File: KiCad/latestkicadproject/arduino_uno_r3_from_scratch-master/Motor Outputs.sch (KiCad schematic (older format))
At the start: 8 parts

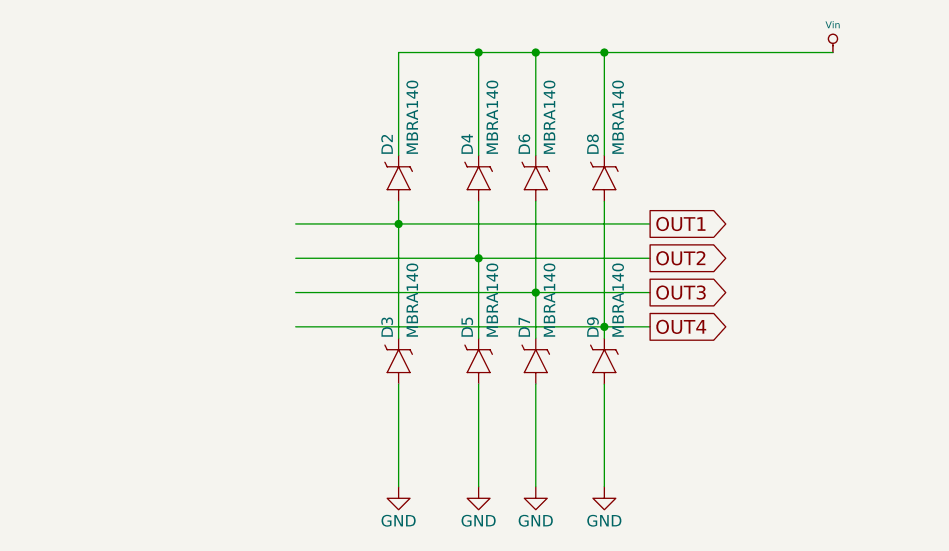
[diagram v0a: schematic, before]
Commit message: 28feb
Aanpassing KiCad+deel footprints
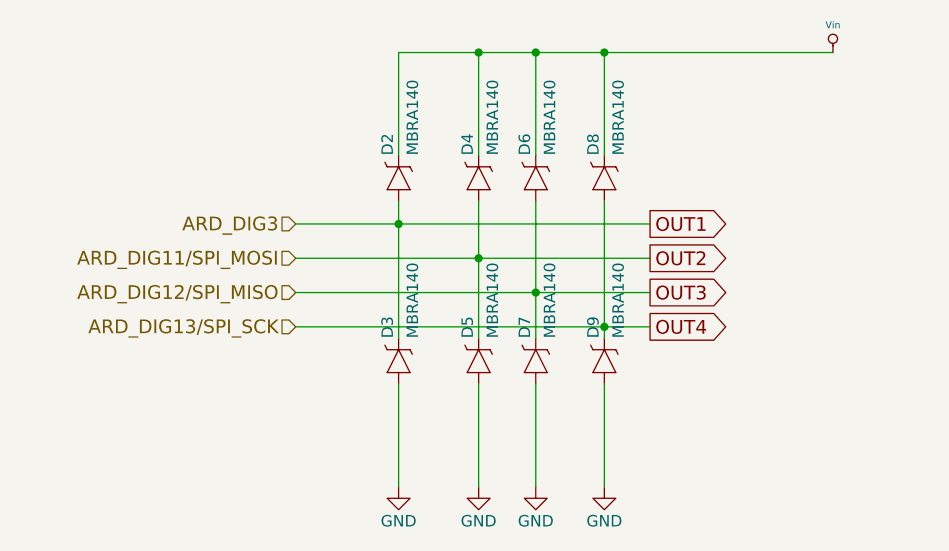
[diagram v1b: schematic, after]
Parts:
- D2, D3, D4, D5, D6, D7, D8, D9: footprint SMA-DIODE -> (none)
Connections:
- net labels added: ARD_DIG11/SPI_MOSI, ARD_DIG12/SPI_MISO, ARD_DIG13/SPI_SCK, ARD_DIG3
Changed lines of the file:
@@
 F 0 "D9" H 6100 4169 50  0000 L BNN
 F 1 "MBRA140" H 6100 4059 50  0000 L BNN
-F 2 "SMA-DIODE" H 6030 4300 20  0001 C CNN
+F 2 "" H 6030 4300 20  0001 C CNN
 F 3 "" H 6000 4150 60  0001 C CNN
 	1    6000 4150
@@
 F 0 "D7" H 5800 4169 50  0000 L BNN
 F 1 "MBRA140" H 5800 4059 50  0000 L BNN
-F 2 "SMA-DIODE" H 5730 4300 20  0001 C CNN
+F 2 "" H 5730 4300 20  0001 C CNN
 F 3 "" H 5700 4150 60  0001 C CNN
 	1    5700 4150
@@
 F 0 "D5" H 5550 4169 50  0000 L BNN
 F 1 "MBRA140" H 5550 4059 50  0000 L BNN
-F 2 "SMA-DIODE" H 5480 4300 20  0001 C CNN
+F 2 "" H 5480 4300 20  0001 C CNN
 F 3 "" H 5450 4150 60  0001 C CNN
 	1    5450 4150
@@
 F 0 "D3" H 5200 4169 50  0000 L BNN
 F 1 "MBRA140" H 5200 4059 50  0000 L BNN
-F 2 "SMA-DIODE" H 5130 4300 20  0001 C CNN
+F 2 "" H 5130 4300 20  0001 C CNN
 F 3 "" H 5100 4150 60  0001 C CNN
 	1    5100 4150
@@
 F 0 "D8" H 6100 3369 50  0000 L BNN
 F 1 "MBRA140" H 6100 3259 50  0000 L BNN
-F 2 "SMA-DIODE" H 6030 3500 20  0001 C CNN
+F 2 "" H 6030 3500 20  0001 C CNN
 F 3 "" H 6000 3350 60  0001 C CNN
 	1    6000 3350
@@
 F 0 "D6" H 5800 3369 50  0000 L BNN
 F 1 "MBRA140" H 5800 3259 50  0000 L BNN
-F 2 "SMA-DIODE" H 5730 3500 20  0001 C CNN
+F 2 "" H 5730 3500 20  0001 C CNN
 F 3 "" H 5700 3350 60  0001 C CNN
 	1    5700 3350
@@
 F 0 "D4" H 5550 3369 50  0000 L BNN
 F 1 "MBRA140" H 5550 3259 50  0000 L BNN
-F 2 "SMA-DIODE" H 5480 3500 20  0001 C CNN
+F 2 "" H 5480 3500 20  0001 C CNN
 F 3 "" H 5450 3350 60  0001 C CNN
 	1    5450 3350
@@
 F 0 "D2" H 5200 3369 50  0000 L BNN
 F 1 "MBRA140" H 5200 3259 50  0000 L BNN
-F 2 "SMA-DIODE" H 5130 3500 20  0001 C CNN
+F 2 "" H 5130 3500 20  0001 C CNN
 F 3 "" H 5100 3350 60  0001 C CNN
 	1    5100 3350
@@
 $EndComp
 $Comp
-L GND #PWR028
+L GND #PWR020
 U 1 1 5A0B3F5C
 P 5100 4700
-F 0 "#PWR028" H 5100 4450 50  0001 C CNN
+F 0 "#PWR020" H 5100 4450 50  0001 C CNN
 F 1 "GND" H 5100 4550 50  0000 C CNN
 F 2 "" H 5100 4700 50  0001 C CNN
@@
 $EndComp
 $Comp
-L GND #PWR029
+L GND #PWR021
 U 1 1 5A0B3F8E
 P 5450 4700
-F 0 "#PWR029" H 5450 4450 50  0001 C CNN
+F 0 "#PWR021" H 5450 4450 50  0001 C CNN
 F 1 "GND" H 5450 4550 50  0000 C CNN
 F 2 "" H 5450 4700 50  0001 C CNN
@@
 $EndComp
 $Comp
-L GND #PWR030
+L GND #PWR022
 U 1 1 5A0B3FB1
 P 5700 4700
-F 0 "#PWR030" H 5700 4450 50  0001 C CNN
+F 0 "#PWR022" H 5700 4450 50  0001 C CNN
 F 1 "GND" H 5700 4550 50  0000 C CNN
 F 2 "" H 5700 4700 50  0001 C CNN
@@
 $EndComp
 $Comp
-L GND #PWR031
+L GND #PWR023
 U 1 1 5A0B43FA
 P 6000 4700
-F 0 "#PWR031" H 6000 4450 50  0001 C CNN
+F 0 "#PWR023" H 6000 4450 50  0001 C CNN
 F 1 "GND" H 6000 4550 50  0000 C CNN
 F 2 "" H 6000 4700 50  0001 C CNN
@@
 Wire Wire Line
 	6000 4250 6000 4700
-Wire Wire Line
-	5450 4700 5450 4250
 Wire Wire Line
 	5700 4250 5700 4700
@@
 Connection ~ 6000 2800
 $Comp
-L Vin #PWR032
+L Vin #PWR024
 U 1 1 5A847DBF
 P 7000 2800
-F 0 "#PWR032" H 7000 2890 20  0001 C CNN
+F 0 "#PWR024" H 7000 2890 20  0001 C CNN
 F 1 "Vin" H 7000 2920 30  0000 C CNN
 F 2 "" H 7000 2800 60  0000 C CNN
@@
 	1    0    0    -1
 $EndComp
+Wire Wire Line
+	5450 4700 5450 4250
+Text HLabel 4650 3550 0    60   Input ~ 0
+ARD_DIG3
+Text HLabel 4650 3700 0    60   Input ~ 0
+ARD_DIG11/SPI_MOSI
+Text HLabel 4650 3850 0    60   Input ~ 0
+ARD_DIG12/SPI_MISO
+Text HLabel 4650 4000 0    60   Input ~ 0
+ARD_DIG13/SPI_SCK
 $EndSCHEMATC

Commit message: Toevoegen footprints Kicad
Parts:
- D2, D3, D4, D5, D6, D7, D8, D9: footprint (none) -> MBRA140:MBRA140TRPBF
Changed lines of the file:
@@
 F 0 "D9" H 6100 4169 50  0000 L BNN
 F 1 "MBRA140" H 6100 4059 50  0000 L BNN
-F 2 "" H 6030 4300 20  0001 C CNN
+F 2 "MBRA140:MBRA140TRPBF" H 6030 4300 20  0001 C CNN
 F 3 "" H 6000 4150 60  0001 C CNN
 	1    6000 4150
@@
 F 0 "D7" H 5800 4169 50  0000 L BNN
 F 1 "MBRA140" H 5800 4059 50  0000 L BNN
-F 2 "" H 5730 4300 20  0001 C CNN
+F 2 "MBRA140:MBRA140TRPBF" H 5730 4300 20  0001 C CNN
 F 3 "" H 5700 4150 60  0001 C CNN
 	1    5700 4150
@@
 F 0 "D5" H 5550 4169 50  0000 L BNN
 F 1 "MBRA140" H 5550 4059 50  0000 L BNN
-F 2 "" H 5480 4300 20  0001 C CNN
+F 2 "MBRA140:MBRA140TRPBF" H 5480 4300 20  0001 C CNN
 F 3 "" H 5450 4150 60  0001 C CNN
 	1    5450 4150
@@
 F 0 "D3" H 5200 4169 50  0000 L BNN
 F 1 "MBRA140" H 5200 4059 50  0000 L BNN
-F 2 "" H 5130 4300 20  0001 C CNN
+F 2 "MBRA140:MBRA140TRPBF" H 5130 4300 20  0001 C CNN
 F 3 "" H 5100 4150 60  0001 C CNN
 	1    5100 4150
@@
 F 0 "D8" H 6100 3369 50  0000 L BNN
 F 1 "MBRA140" H 6100 3259 50  0000 L BNN
-F 2 "" H 6030 3500 20  0001 C CNN
+F 2 "MBRA140:MBRA140TRPBF" H 6030 3500 20  0001 C CNN
 F 3 "" H 6000 3350 60  0001 C CNN
 	1    6000 3350
@@
 F 0 "D6" H 5800 3369 50  0000 L BNN
 F 1 "MBRA140" H 5800 3259 50  0000 L BNN
-F 2 "" H 5730 3500 20  0001 C CNN
+F 2 "MBRA140:MBRA140TRPBF" H 5730 3500 20  0001 C CNN
 F 3 "" H 5700 3350 60  0001 C CNN
 	1    5700 3350
@@
 F 0 "D4" H 5550 3369 50  0000 L BNN
 F 1 "MBRA140" H 5550 3259 50  0000 L BNN
-F 2 "" H 5480 3500 20  0001 C CNN
+F 2 "MBRA140:MBRA140TRPBF" H 5480 3500 20  0001 C CNN
 F 3 "" H 5450 3350 60  0001 C CNN
 	1    5450 3350
@@
 F 0 "D2" H 5200 3369 50  0000 L BNN
 F 1 "MBRA140" H 5200 3259 50  0000 L BNN
-F 2 "" H 5130 3500 20  0001 C CNN
+F 2 "MBRA140:MBRA140TRPBF" H 5130 3500 20  0001 C CNN
 F 3 "" H 5100 3350 60  0001 C CNN
 	1    5100 3350

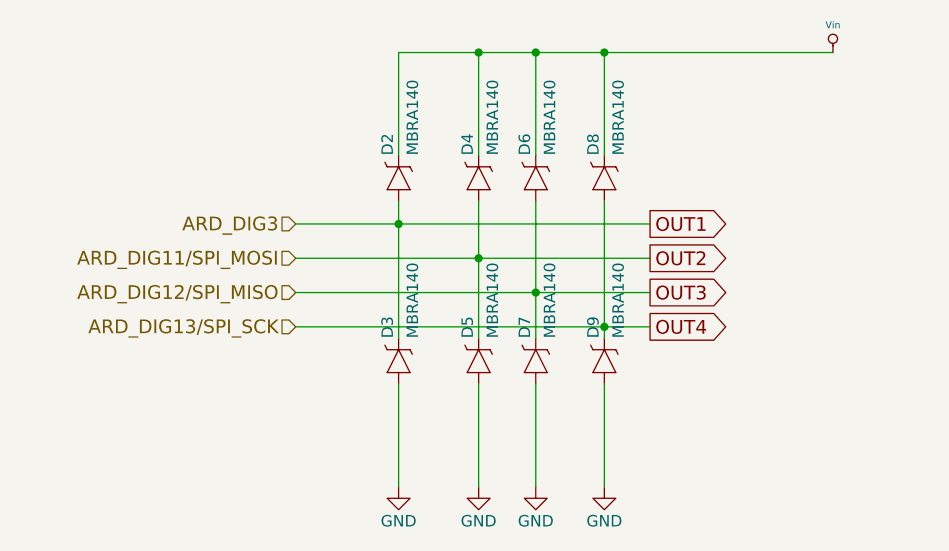
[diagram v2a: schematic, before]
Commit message: Aanpassing KiCad PCB ontwerp + footprints
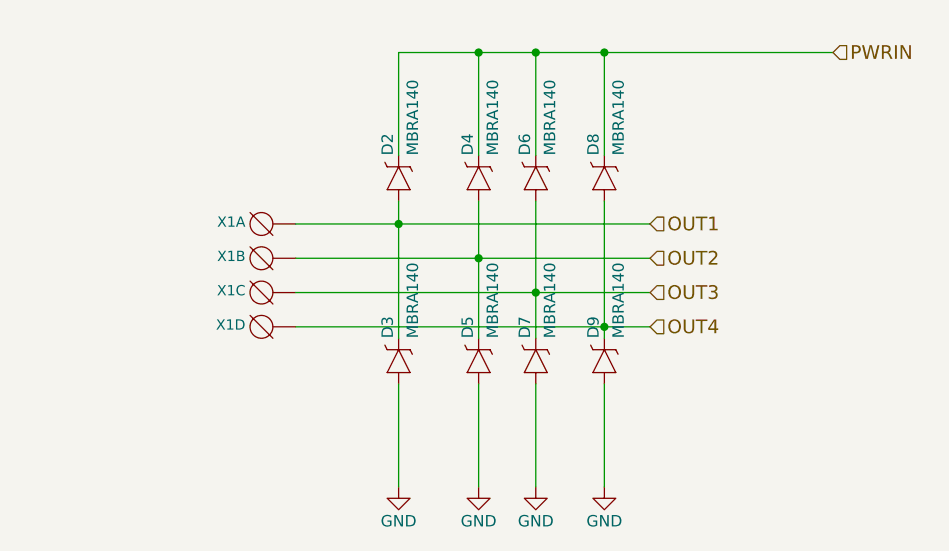
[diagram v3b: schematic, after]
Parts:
- added X1: DG3XX-04-3.5, degson:degson-DG350-3.5-04P, symbol DG3XX-04-3.5
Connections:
- net OUT1: now also X1.1 (KL)
- net OUT2: now also X1.2 (KL)
- net OUT3: now also X1.3 (KL)
- net OUT4: now also X1.4 (KL)
- net PWRIN: now reaches D2.C, D4.C, D6.C, D8.C
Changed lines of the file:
@@
 LIBS:l298A
 LIBS:Arduino_Uno_R3_From_Scratch-cache
+LIBS:battery
+LIBS:MC33269ST
+LIBS:LP2985-33DBVR
+LIBS:degson
 EELAYER 25 0
 EELAYER END
 $Descr A4 11693 8268
 encoding utf-8
-Sheet 6 7
+Sheet 4 6
 Title ""
 Date ""
@@
 Comment4 ""
 $EndDescr
-Text GLabel 6200 4000 2    60   Output ~ 0
-OUT4
-Text GLabel 6200 3850 2    60   Output ~ 0
-OUT3
-Text GLabel 6200 3700 2    60   Output ~ 0
-OUT2
-Text GLabel 6200 3550 2    60   Output ~ 0
-OUT1
 $Comp
 L MBRA140 D9
@@
 $EndComp
 $Comp
-L GND #PWR020
+L GND #PWR011
 U 1 1 5A0B3F5C
 P 5100 4700
-F 0 "#PWR020" H 5100 4450 50  0001 C CNN
+F 0 "#PWR011" H 5100 4450 50  0001 C CNN
 F 1 "GND" H 5100 4550 50  0000 C CNN
 F 2 "" H 5100 4700 50  0001 C CNN
@@
 $EndComp
 $Comp
-L GND #PWR021
+L GND #PWR012
 U 1 1 5A0B3F8E
 P 5450 4700
-F 0 "#PWR021" H 5450 4450 50  0001 C CNN
+F 0 "#PWR012" H 5450 4450 50  0001 C CNN
 F 1 "GND" H 5450 4550 50  0000 C CNN
 F 2 "" H 5450 4700 50  0001 C CNN
@@
 $EndComp
 $Comp
-L GND #PWR022
+L GND #PWR013
 U 1 1 5A0B3FB1
 P 5700 4700
-F 0 "#PWR022" H 5700 4450 50  0001 C CNN
+F 0 "#PWR013" H 5700 4450 50  0001 C CNN
 F 1 "GND" H 5700 4550 50  0000 C CNN
 F 2 "" H 5700 4700 50  0001 C CNN
@@
 $EndComp
 $Comp
-L GND #PWR023
+L GND #PWR014
 U 1 1 5A0B43FA
 P 6000 4700
-F 0 "#PWR023" H 6000 4450 50  0001 C CNN
+F 0 "#PWR014" H 6000 4450 50  0001 C CNN
 F 1 "GND" H 6000 4550 50  0000 C CNN
 F 2 "" H 6000 4700 50  0001 C CNN
@@
 	6000 3250 6000 2800
 Connection ~ 6000 2800
-$Comp
-L Vin #PWR024
-U 1 1 5A847DBF
-P 7000 2800
-F 0 "#PWR024" H 7000 2890 20  0001 C CNN
-F 1 "Vin" H 7000 2920 30  0000 C CNN
-F 2 "" H 7000 2800 60  0000 C CNN
-F 3 "" H 7000 2800 60  0000 C CNN
-	1    7000 2800
-	1    0    0    -1
-$EndComp
 Wire Wire Line
 	5450 4700 5450 4250
-Text HLabel 4650 3550 0    60   Input ~ 0
-ARD_DIG3
-Text HLabel 4650 3700 0    60   Input ~ 0
-ARD_DIG11/SPI_MOSI
-Text HLabel 4650 3850 0    60   Input ~ 0
-ARD_DIG12/SPI_MISO
-Text HLabel 4650 4000 0    60   Input ~ 0
-ARD_DIG13/SPI_SCK
+Text HLabel 7000 2800 2    60   Input ~ 0
+PWRIN
+Text HLabel 6200 3550 2    60   Input ~ 0
+OUT1
+Text HLabel 6200 3700 2    60   Input ~ 0
+OUT2
+Text HLabel 6200 3850 2    60   Input ~ 0
+OUT3
+Text HLabel 6200 4000 2    60   Input ~ 0
+OUT4
+$Comp
+L DG3XX-04-3.5 X1
+U 1 1 5AA3CE64
+P 4550 3550
+F 0 "X1" H 4670 3515 45  0000 L BNN
+F 1 "DG3XX-04-3.5" H 4550 3550 45  0001 L BNN
+F 2 "degson:degson-DG350-3.5-04P" H 4580 3700 20  0001 C CNN
+F 3 "" H 4550 3550 60  0001 C CNN
+	1    4550 3550
+	-1   0    0    1
+$EndComp
+$Comp
+L DG3XX-04-3.5 X1
+U 2 1 5AA3CEDB
+P 4550 3700
+F 0 "X1" H 4670 3665 45  0000 L BNN
+F 1 "DG3XX-04-3.5" H 4550 3700 45  0001 L BNN
+F 2 "degson:degson-DG350-3.5-04P" H 4580 3850 20  0001 C CNN
+F 3 "" H 4550 3700 60  0001 C CNN
+	2    4550 3700
+	-1   0    0    1
+$EndComp
+$Comp
+L DG3XX-04-3.5 X1
+U 3 1 5AA3CF1C
+P 4550 3850
+F 0 "X1" H 4670 3815 45  0000 L BNN
+F 1 "DG3XX-04-3.5" H 4550 3850 45  0001 L BNN
+F 2 "degson:degson-DG350-3.5-04P" H 4580 4000 20  0001 C CNN
+F 3 "" H 4550 3850 60  0001 C CNN
+	3    4550 3850
+	-1   0    0    1
+$EndComp
+$Comp
+L DG3XX-04-3.5 X1
+U 4 1 5AA3CF7F
+P 4550 4000
+F 0 "X1" H 4670 3965 45  0000 L BNN
+F 1 "DG3XX-04-3.5" H 4550 4000 45  0001 L BNN
+F 2 "degson:degson-DG350-3.5-04P" H 4580 4150 20  0001 C CNN
+F 3 "" H 4550 4000 60  0001 C CNN
+	4    4550 4000
+	-1   0    0    1
+$EndComp
 $EndSCHEMATC

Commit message: pcb routing
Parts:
- removed D2, D3, D4, D5, D6, D7, D8, D9: MBRA140, MBRA140:MBRA140TRPBF, symbol MBRA140
- added D2, D3, D4, D5, D6, D7, D8, D9: D, Diodes_SMD:D_MicroMELF_Hadsoldering, symbol D
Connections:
- net GND: now also D3.2 (A), D5.2 (A), D7.2 (A), D9.2 (A)
- net OUT1: now also D2.2 (A), D3.1 (K)
- net OUT2: now also D4.2 (A), D5.1 (K)
- net OUT3: now also D6.2 (A), D7.1 (K)
- net OUT4: now also D8.2 (A), D9.1 (K)
- net PWRIN: now also D2.1 (K), D4.1 (K), D6.1 (K), D8.1 (K)
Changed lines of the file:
@@
 LIBS:LP2985-33DBVR
 LIBS:degson
+LIBS:PHT6NQ10T_135
 EELAYER 25 0
 EELAYER END
@@
 $EndDescr
 $Comp
-L MBRA140 D9
-U 1 1 5A047FE0
-P 6000 4150
-F 0 "D9" H 6100 4169 50  0000 L BNN
-F 1 "MBRA140" H 6100 4059 50  0000 L BNN
-F 2 "MBRA140:MBRA140TRPBF" H 6030 4300 20  0001 C CNN
-F 3 "" H 6000 4150 60  0001 C CNN
-	1    6000 4150
-	0    -1   -1   0
-$EndComp
-$Comp
-L MBRA140 D7
-U 1 1 5A0480F2
-P 5700 4150
-F 0 "D7" H 5800 4169 50  0000 L BNN
-F 1 "MBRA140" H 5800 4059 50  0000 L BNN
-F 2 "MBRA140:MBRA140TRPBF" H 5730 4300 20  0001 C CNN
-F 3 "" H 5700 4150 60  0001 C CNN
-	1    5700 4150
-	0    -1   -1   0
-$EndComp
-$Comp
-L MBRA140 D5
-U 1 1 5A04816A
-P 5450 4150
-F 0 "D5" H 5550 4169 50  0000 L BNN
-F 1 "MBRA140" H 5550 4059 50  0000 L BNN
-F 2 "MBRA140:MBRA140TRPBF" H 5480 4300 20  0001 C CNN
-F 3 "" H 5450 4150 60  0001 C CNN
-	1    5450 4150
-	0    -1   -1   0
-$EndComp
-$Comp
-L MBRA140 D3
-U 1 1 5A0481B3
-P 5100 4150
-F 0 "D3" H 5200 4169 50  0000 L BNN
-F 1 "MBRA140" H 5200 4059 50  0000 L BNN
-F 2 "MBRA140:MBRA140TRPBF" H 5130 4300 20  0001 C CNN
-F 3 "" H 5100 4150 60  0001 C CNN
-	1    5100 4150
-	0    -1   -1   0
-$EndComp
-$Comp
-L MBRA140 D8
-U 1 1 5A04820B
-P 6000 3350
-F 0 "D8" H 6100 3369 50  0000 L BNN
-F 1 "MBRA140" H 6100 3259 50  0000 L BNN
-F 2 "MBRA140:MBRA140TRPBF" H 6030 3500 20  0001 C CNN
-F 3 "" H 6000 3350 60  0001 C CNN
-	1    6000 3350
-	0    -1   -1   0
-$EndComp
-$Comp
-L MBRA140 D6
-U 1 1 5A0482B1
-P 5700 3350
-F 0 "D6" H 5800 3369 50  0000 L BNN
-F 1 "MBRA140" H 5800 3259 50  0000 L BNN
-F 2 "MBRA140:MBRA140TRPBF" H 5730 3500 20  0001 C CNN
-F 3 "" H 5700 3350 60  0001 C CNN
-	1    5700 3350
-	0    -1   -1   0
-$EndComp
-$Comp
-L MBRA140 D4
-U 1 1 5A0482E5
-P 5450 3350
-F 0 "D4" H 5550 3369 50  0000 L BNN
-F 1 "MBRA140" H 5550 3259 50  0000 L BNN
-F 2 "MBRA140:MBRA140TRPBF" H 5480 3500 20  0001 C CNN
-F 3 "" H 5450 3350 60  0001 C CNN
-	1    5450 3350
-	0    -1   -1   0
-$EndComp
-$Comp
-L MBRA140 D2
-U 1 1 5A048318
-P 5100 3350
-F 0 "D2" H 5200 3369 50  0000 L BNN
-F 1 "MBRA140" H 5200 3259 50  0000 L BNN
-F 2 "MBRA140:MBRA140TRPBF" H 5130 3500 20  0001 C CNN
-F 3 "" H 5100 3350 60  0001 C CNN
-	1    5100 3350
-	0    -1   -1   0
-$EndComp
-$Comp
 L GND #PWR011
 U 1 1 5A0B3F5C
@@
 	4650 3550 6200 3550
 Wire Wire Line
-	5100 4250 5100 4700
-Wire Wire Line
-	6000 4250 6000 4700
-Wire Wire Line
-	5700 4250 5700 4700
-Wire Wire Line
 	5100 3450 5100 4050
 Connection ~ 5100 3550
@@
 Connection ~ 6000 4000
 Wire Wire Line
-	5100 3250 5100 2800
-Wire Wire Line
 	5100 2800 7000 2800
-Wire Wire Line
-	5450 3250 5450 2800
 Connection ~ 5450 2800
-Wire Wire Line
-	5700 3250 5700 2800
 Connection ~ 5700 2800
-Wire Wire Line
-	6000 3250 6000 2800
 Connection ~ 6000 2800
-Wire Wire Line
-	5450 4700 5450 4250
 Text HLabel 7000 2800 2    60   Input ~ 0
 PWRIN
@@
 	-1   0    0    1
 $EndComp
+$Comp
+L D D2
+U 1 1 5AA7D6C2
+P 5100 3300
+F 0 "D2" H 5100 3400 50  0000 C CNN
+F 1 "D" H 5100 3200 50  0000 C CNN
+F 2 "Diodes_SMD:D_MicroMELF_Hadsoldering" H 5100 3300 50  0001 C CNN
+F 3 "" H 5100 3300 50  0001 C CNN
+	1    5100 3300
+	0    1    1    0
+$EndComp
+$Comp
+L D D4
+U 1 1 5AA7D743
+P 5450 3300
+F 0 "D4" H 5450 3400 50  0000 C CNN
+F 1 "D" H 5450 3200 50  0000 C CNN
+F 2 "Diodes_SMD:D_MicroMELF_Hadsoldering" H 5450 3300 50  0001 C CNN
+F 3 "" H 5450 3300 50  0001 C CNN
+	1    5450 3300
+	0    1    1    0
+$EndComp
+$Comp
+L D D6
+U 1 1 5AA7D774
+P 5700 3300
+F 0 "D6" H 5700 3400 50  0000 C CNN
+F 1 "D" H 5700 3200 50  0000 C CNN
+F 2 "Diodes_SMD:D_MicroMELF_Hadsoldering" H 5700 3300 50  0001 C CNN
+F 3 "" H 5700 3300 50  0001 C CNN
+	1    5700 3300
+	0    1    1    0
+$EndComp
+$Comp
+L D D8
+U 1 1 5AA7D7A7
+P 6000 3300
+F 0 "D8" H 6000 3400 50  0000 C CNN
+F 1 "D" H 6000 3200 50  0000 C CNN
+F 2 "Diodes_SMD:D_MicroMELF_Hadsoldering" H 6000 3300 50  0001 C CNN
+F 3 "" H 6000 3300 50  0001 C CNN
+	1    6000 3300
+	0    1    1    0
+$EndComp
+Wire Wire Line
+	5100 3150 5100 2800
+Wire Wire Line
+	5450 3150 5450 2800
+Wire Wire Line
+	5700 3150 5700 2800
+Wire Wire Line
+	6000 3150 6000 2800
+$Comp
+L D D9
+U 1 1 5AA7F90A
+P 6000 4200
+F 0 "D9" H 6000 4300 50  0000 C CNN
+F 1 "D" H 6000 4100 50  0000 C CNN
+F 2 "Diodes_SMD:D_MicroMELF_Hadsoldering" H 6000 4200 50  0001 C CNN
+F 3 "" H 6000 4200 50  0001 C CNN
+	1    6000 4200
+	0    1    1    0
+$EndComp
+$Comp
+L D D7
+U 1 1 5AA7F96F
+P 5700 4200
+F 0 "D7" H 5700 4300 50  0000 C CNN
+F 1 "D" H 5700 4100 50  0000 C CNN
+F 2 "Diodes_SMD:D_MicroMELF_Hadsoldering" H 5700 4200 50  0001 C CNN
+F 3 "" H 5700 4200 50  0001 C CNN
+	1    5700 4200
+	0    1    1    0
+$EndComp
+$Comp
+L D D5
+U 1 1 5AA7F99A
+P 5450 4200
+F 0 "D5" H 5450 4300 50  0000 C CNN
+F 1 "D" H 5450 4100 50  0000 C CNN
+F 2 "Diodes_SMD:D_MicroMELF_Hadsoldering" H 5450 4200 50  0001 C CNN
+F 3 "" H 5450 4200 50  0001 C CNN
+	1    5450 4200
+	0    1    1    0
+$EndComp
+$Comp
+L D D3
+U 1 1 5AA7FA31
+P 5100 4200
+F 0 "D3" H 5100 4300 50  0000 C CNN
+F 1 "D" H 5100 4100 50  0000 C CNN
+F 2 "Diodes_SMD:D_MicroMELF_Hadsoldering" H 5100 4200 50  0001 C CNN
+F 3 "" H 5100 4200 50  0001 C CNN
+	1    5100 4200
+	0    1    1    0
+$EndComp
+Wire Wire Line
+	5100 4350 5100 4700
+Wire Wire Line
+	5450 4350 5450 4700
+Wire Wire Line
+	5700 4350 5700 4700
+Wire Wire Line
+	6000 4700 6000 4350
 $EndSCHEMATC

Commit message: PCB routing v1
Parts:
- D2, D3, D4, D5, D6, D7, D8, D9: footprint Diodes_SMD:D_MicroMELF_Hadsoldering -> SK25AHM2G:DIOM5437X240N
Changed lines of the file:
@@
 LIBS:degson
 LIBS:PHT6NQ10T_135
+LIBS:L298P
 EELAYER 25 0
 EELAYER END
@@
 $EndDescr
 $Comp
-L GND #PWR011
+L GND #PWR014
 U 1 1 5A0B3F5C
 P 5100 4700
-F 0 "#PWR011" H 5100 4450 50  0001 C CNN
+F 0 "#PWR014" H 5100 4450 50  0001 C CNN
 F 1 "GND" H 5100 4550 50  0000 C CNN
 F 2 "" H 5100 4700 50  0001 C CNN
@@
 $EndComp
 $Comp
-L GND #PWR012
+L GND #PWR015
 U 1 1 5A0B3F8E
 P 5450 4700
-F 0 "#PWR012" H 5450 4450 50  0001 C CNN
+F 0 "#PWR015" H 5450 4450 50  0001 C CNN
 F 1 "GND" H 5450 4550 50  0000 C CNN
 F 2 "" H 5450 4700 50  0001 C CNN
@@
 $EndComp
 $Comp
-L GND #PWR013
+L GND #PWR016
 U 1 1 5A0B3FB1
 P 5700 4700
-F 0 "#PWR013" H 5700 4450 50  0001 C CNN
+F 0 "#PWR016" H 5700 4450 50  0001 C CNN
 F 1 "GND" H 5700 4550 50  0000 C CNN
 F 2 "" H 5700 4700 50  0001 C CNN
@@
 $EndComp
 $Comp
-L GND #PWR014
+L GND #PWR017
 U 1 1 5A0B43FA
 P 6000 4700
-F 0 "#PWR014" H 6000 4450 50  0001 C CNN
+F 0 "#PWR017" H 6000 4450 50  0001 C CNN
 F 1 "GND" H 6000 4550 50  0000 C CNN
 F 2 "" H 6000 4700 50  0001 C CNN
@@
 F 0 "D2" H 5100 3400 50  0000 C CNN
 F 1 "D" H 5100 3200 50  0000 C CNN
-F 2 "Diodes_SMD:D_MicroMELF_Hadsoldering" H 5100 3300 50  0001 C CNN
+F 2 "SK25AHM2G:DIOM5437X240N" H 5100 3300 50  0001 C CNN
 F 3 "" H 5100 3300 50  0001 C CNN
 	1    5100 3300
@@
 F 0 "D4" H 5450 3400 50  0000 C CNN
 F 1 "D" H 5450 3200 50  0000 C CNN
-F 2 "Diodes_SMD:D_MicroMELF_Hadsoldering" H 5450 3300 50  0001 C CNN
+F 2 "SK25AHM2G:DIOM5437X240N" H 5450 3300 50  0001 C CNN
 F 3 "" H 5450 3300 50  0001 C CNN
 	1    5450 3300
@@
 F 0 "D6" H 5700 3400 50  0000 C CNN
 F 1 "D" H 5700 3200 50  0000 C CNN
-F 2 "Diodes_SMD:D_MicroMELF_Hadsoldering" H 5700 3300 50  0001 C CNN
+F 2 "SK25AHM2G:DIOM5437X240N" H 5700 3300 50  0001 C CNN
 F 3 "" H 5700 3300 50  0001 C CNN
 	1    5700 3300
@@
 F 0 "D8" H 6000 3400 50  0000 C CNN
 F 1 "D" H 6000 3200 50  0000 C CNN
-F 2 "Diodes_SMD:D_MicroMELF_Hadsoldering" H 6000 3300 50  0001 C CNN
+F 2 "SK25AHM2G:DIOM5437X240N" H 6000 3300 50  0001 C CNN
 F 3 "" H 6000 3300 50  0001 C CNN
 	1    6000 3300
@@
 F 0 "D9" H 6000 4300 50  0000 C CNN
 F 1 "D" H 6000 4100 50  0000 C CNN
-F 2 "Diodes_SMD:D_MicroMELF_Hadsoldering" H 6000 4200 50  0001 C CNN
+F 2 "SK25AHM2G:DIOM5437X240N" H 6000 4200 50  0001 C CNN
 F 3 "" H 6000 4200 50  0001 C CNN
 	1    6000 4200
@@
 F 0 "D7" H 5700 4300 50  0000 C CNN
 F 1 "D" H 5700 4100 50  0000 C CNN
-F 2 "Diodes_SMD:D_MicroMELF_Hadsoldering" H 5700 4200 50  0001 C CNN
+F 2 "SK25AHM2G:DIOM5437X240N" H 5700 4200 50  0001 C CNN
 F 3 "" H 5700 4200 50  0001 C CNN
 	1    5700 4200
@@
 F 0 "D5" H 5450 4300 50  0000 C CNN
 F 1 "D" H 5450 4100 50  0000 C CNN
-F 2 "Diodes_SMD:D_MicroMELF_Hadsoldering" H 5450 4200 50  0001 C CNN
+F 2 "SK25AHM2G:DIOM5437X240N" H 5450 4200 50  0001 C CNN
 F 3 "" H 5450 4200 50  0001 C CNN
 	1    5450 4200
@@
 F 0 "D3" H 5100 4300 50  0000 C CNN
 F 1 "D" H 5100 4100 50  0000 C CNN
-F 2 "Diodes_SMD:D_MicroMELF_Hadsoldering" H 5100 4200 50  0001 C CNN
+F 2 "SK25AHM2G:DIOM5437X240N" H 5100 4200 50  0001 C CNN
 F 3 "" H 5100 4200 50  0001 C CNN
 	1    5100 4200
